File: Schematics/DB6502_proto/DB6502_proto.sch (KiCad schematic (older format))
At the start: 22 parts, among them SW1 Reset, U1 DS1813, U2 65C02S, U3 62256, U4 ATmega644PA-PU, U5 62256, U6 74AC138, U7 28C256, U8 22V10C, Y1 20MHz

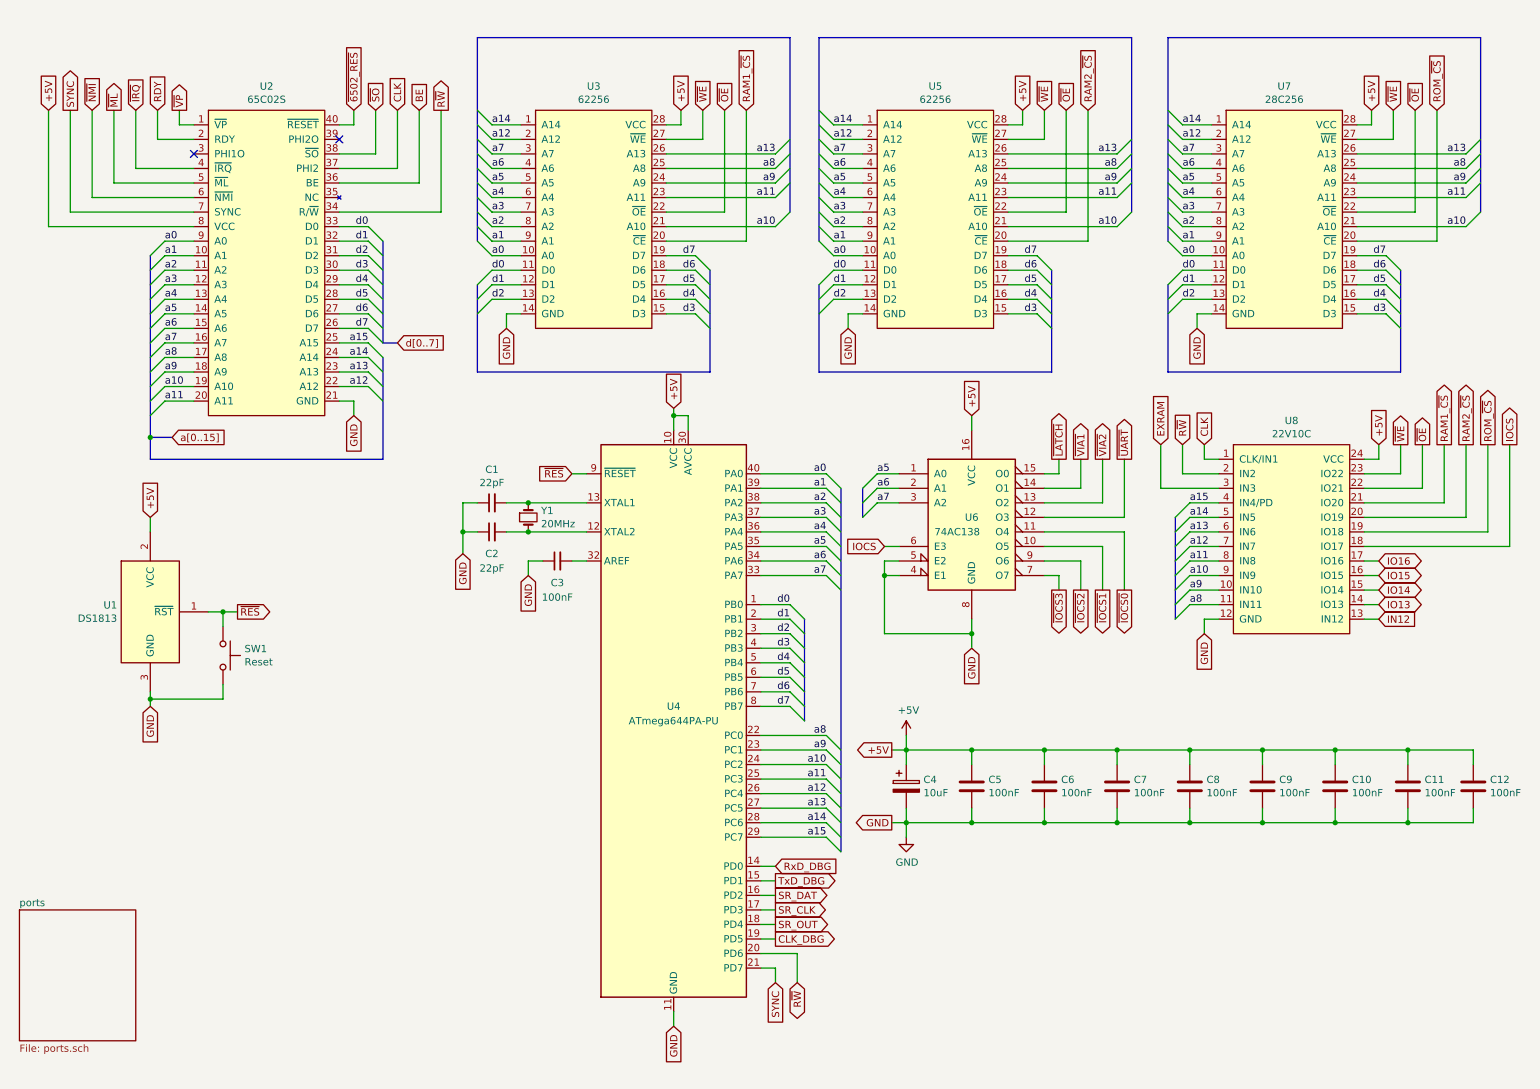
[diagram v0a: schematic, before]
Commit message: Started documenting current system layout
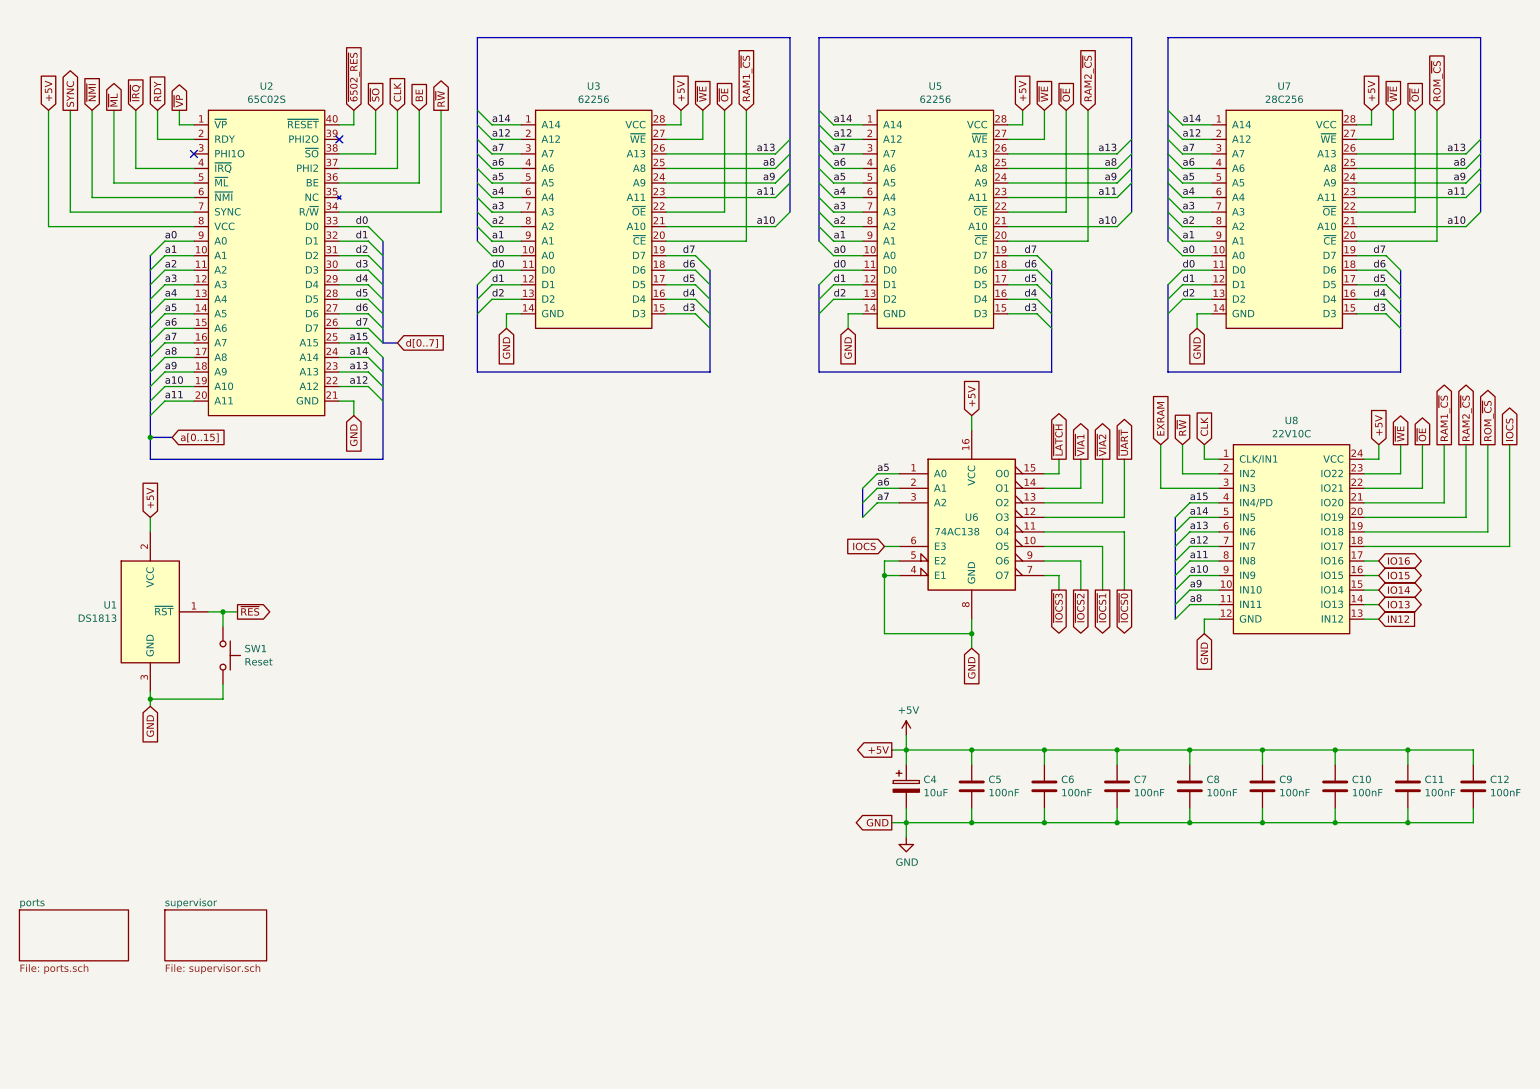
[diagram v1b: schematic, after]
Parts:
- removed C1, C2: 22pF, Capacitor_THT:C_Disc_D5.0mm_W2.5mm_P2.50mm, symbol Device:C_Small
- removed C3: 100nF, Capacitor_THT:C_Disc_D5.0mm_W2.5mm_P2.50mm, symbol Device:C_Small
- removed U4: ATmega644PA-PU, Package_DIP:DIP-40_W15.24mm_Socket, symbol MCU_Microchip_ATmega:ATmega644PA-PU
- removed Y1: 20MHz, Crystal:Crystal_HC49-U_Vertical, symbol Device:Crystal_Small

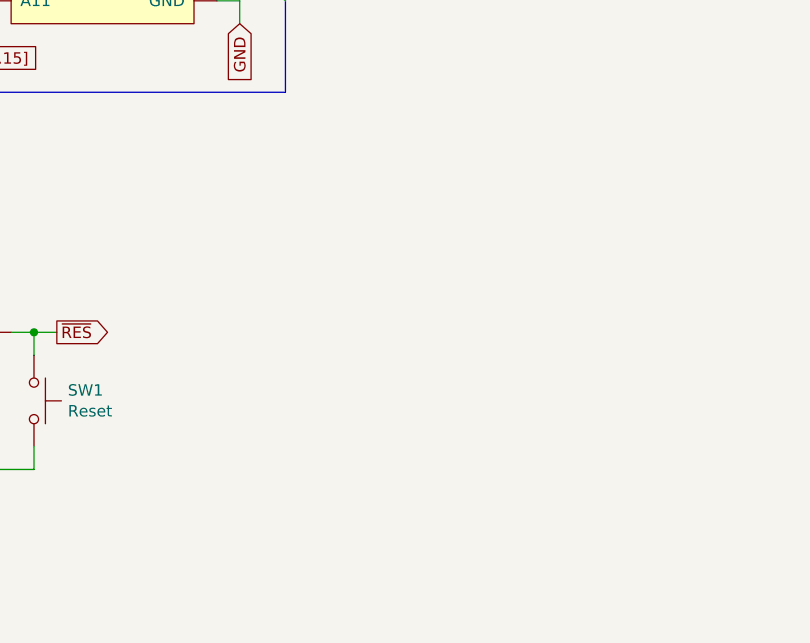
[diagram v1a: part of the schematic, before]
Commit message: Updated supervisor schematic
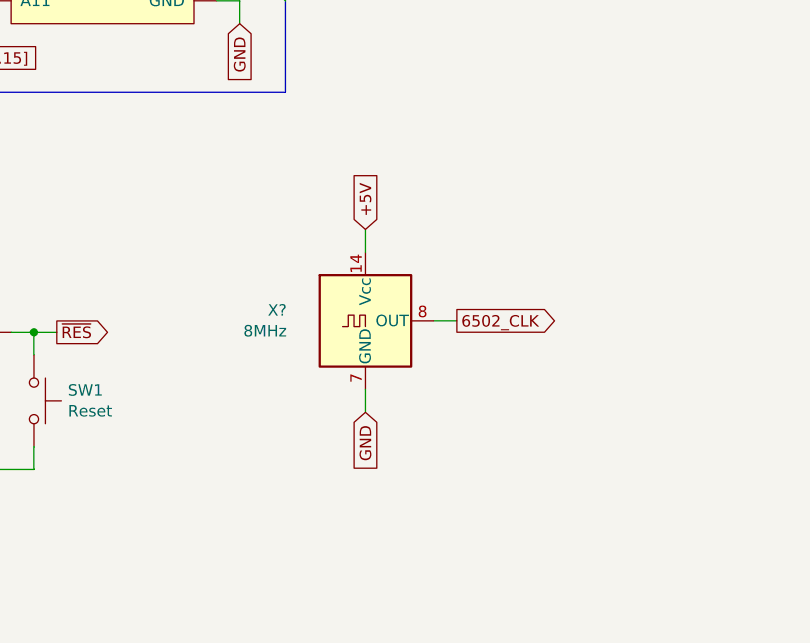
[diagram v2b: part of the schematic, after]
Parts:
- added X?: 8MHz, Oscillator:Oscillator_DIP-14, symbol Oscillator:ACO-xxxMHz
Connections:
- net +5V: now also X?.14 (Vcc)
- net GND: now also X?.7 (GND)
- new net 6502_CLK: X?.8 (OUT)
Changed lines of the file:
@@
 Text GLabel 6650 4150 0    50   Input ~ 0
 IOCS
+$Comp
+L Oscillator:ACO-xxxMHz X?
+U 1 1 5F9BC711
+P 3550 4550
+F 0 "X?" H 3206 4596 50  0000 R CNN
+F 1 "8MHz" H 3206 4505 50  0000 R CNN
+F 2 "Oscillator:Oscillator_DIP-14" H 4000 4200 50  0001 C CNN
+F 3 "" H 3450 4550 50  0001 C CNN
+	1    3550 4550
+	1    0    0    -1
+$EndComp
+Text GLabel 3550 4150 1    50   Input ~ 0
++5V
+Text GLabel 3550 4950 3    50   Input ~ 0
+GND
+Text GLabel 3950 4550 2    50   Output ~ 0
+6502_CLK
+Wire Wire Line
+	3550 4150 3550 4250
+Wire Wire Line
+	3550 4950 3550 4850
+Wire Wire Line
+	3850 4550 3950 4550
 Wire Bus Line
 	6500 3750 6500 3950

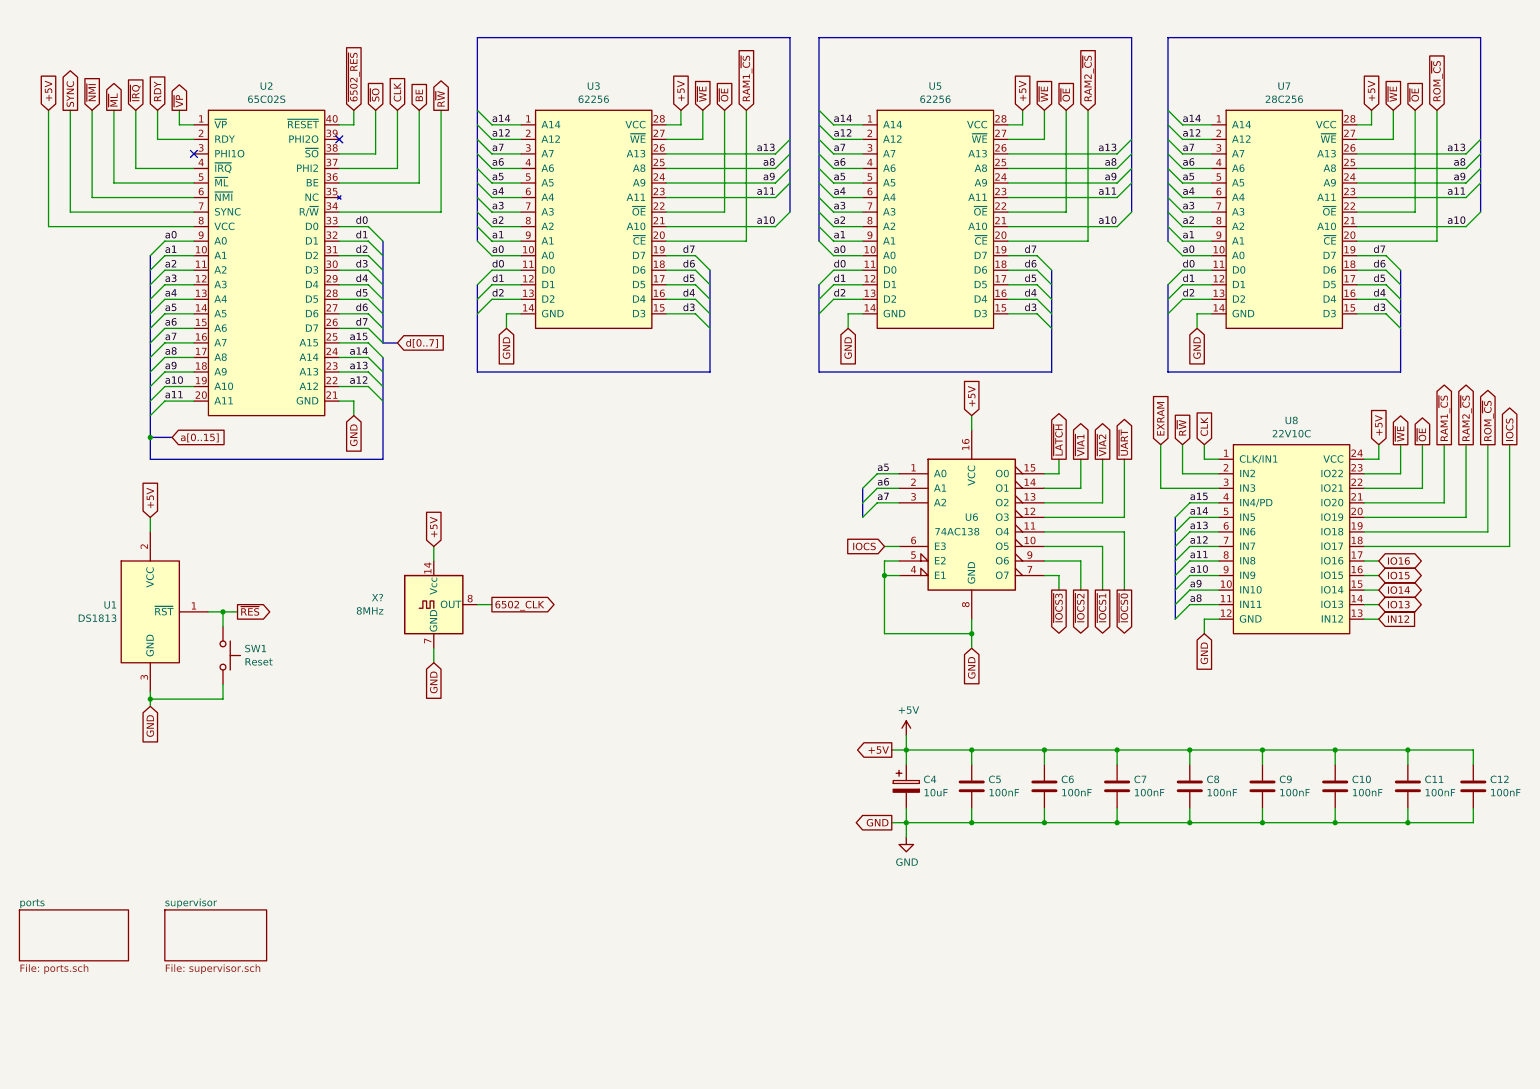
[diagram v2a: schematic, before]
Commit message: Implemented wait state generator, cleaned up schematic
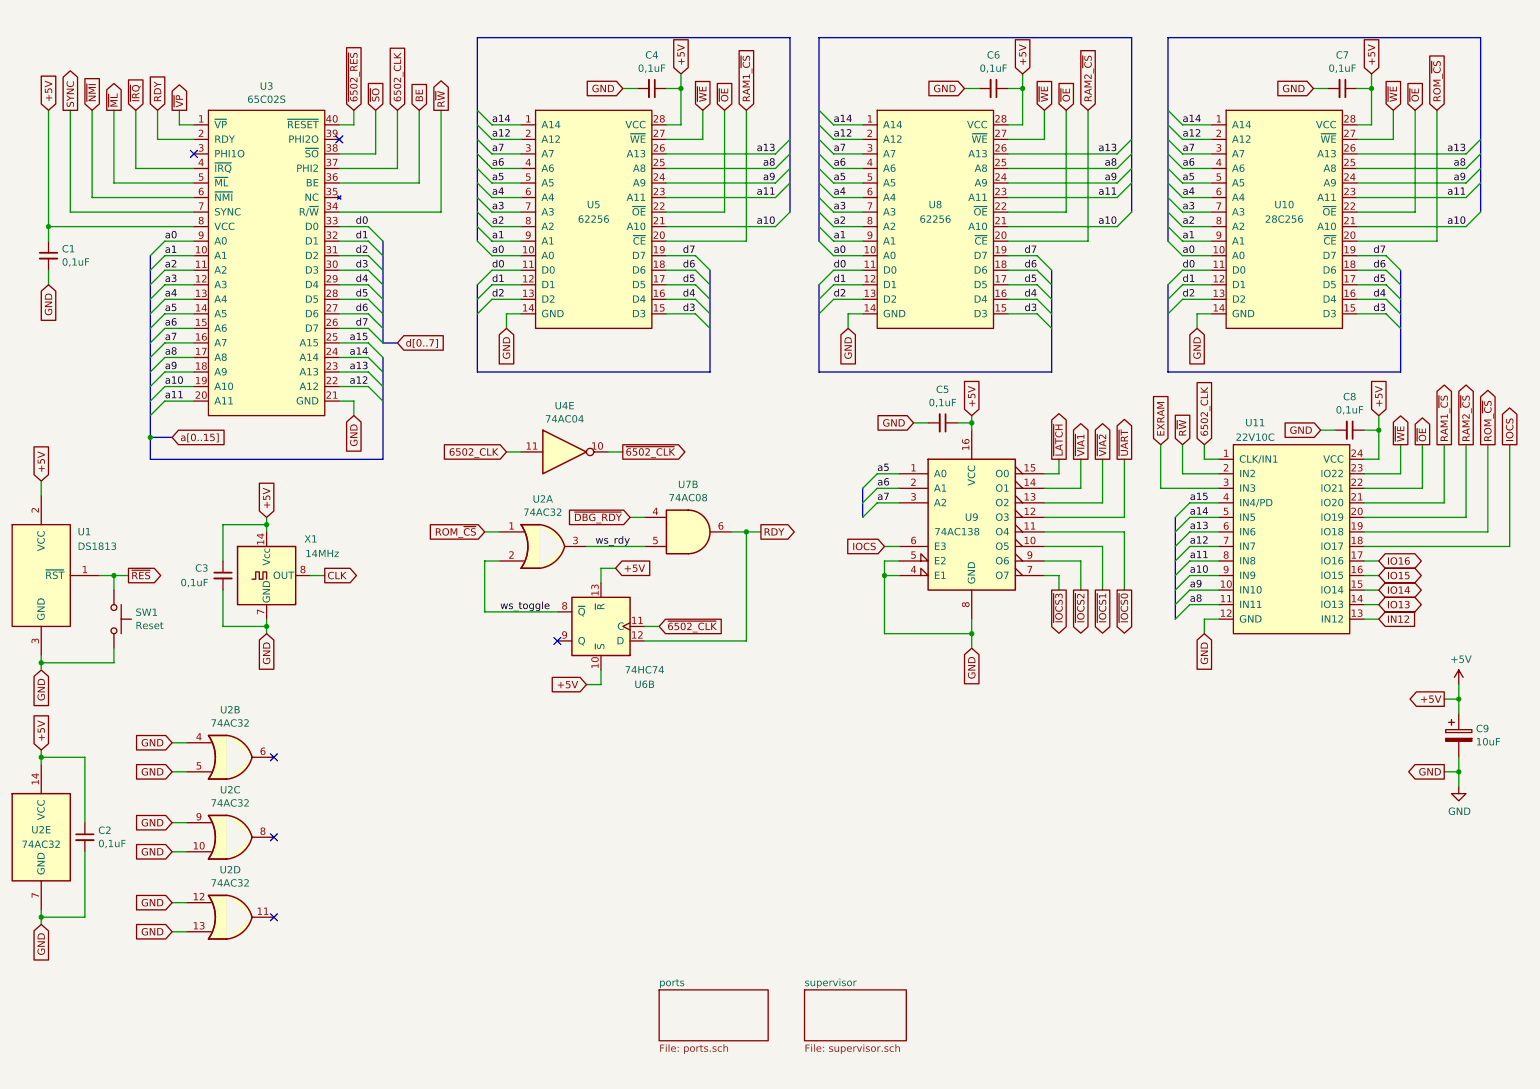
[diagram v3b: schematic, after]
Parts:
- removed C10, C11, C12, C5, C6, C7, C8, C9: 100nF, Capacitor_THT:C_Disc_D5.0mm_W2.5mm_P2.50mm, symbol Device:C
- added C1, C2, C3, C4, C5, C6, C7, C8: 0,1uF, symbol Device:C_Small
- added U2: 74AC32, symbol 74xx:74LS32
- added U4: 74AC04, symbol 74xx:74LS04
- added U6: 74HC74, symbol 74xx:74HC74
- added U7: 74AC08, symbol 74xx:74LS08
- X1: renamed from X?; value 8MHz -> 14MHz
- renumbered C4 to C9, U7 to U10, U8 to U11, U2 to U3, U3 to U5, U5 to U8, U6 to U9
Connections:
- net +5V: now also C1.1, C2.1, C3.1, C4.1, C5.1, C6.1, C7.1, C8.1, U2.14 (VCC), U6.10 (~S), U6.13 (~R)
- net 6502_CLK: now also U11.1 (CLK/IN1), U3.37 (PHI2), U4.11; no longer X1.8 (OUT)
- net CLK: now also X1.8 (OUT); no longer U11.1 (CLK/IN1), U3.37 (PHI2)
- net GND: now also C1.2, C2.2, C3.2, C4.2, C5.2, C6.2, C7.2, C8.2, U2.10, U2.12, U2.13, U2.4, U2.5, U2.7 (GND), U2.9
- net RDY: now also U6.12 (D), U7.6
- net ROM_~CS: now also U2.1
- new net ws_rdy: U2.3, U7.5
- new net ws_toggle: U2.2, U6.8 (~Q)
- new net ~6502_CLK: U4.10, U6.11 (C)
- new net ~DBG_RDY: U7.4
- no-connect marks 2 -> 6
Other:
- moved on the sheet: C9, SW1, U1, X1
